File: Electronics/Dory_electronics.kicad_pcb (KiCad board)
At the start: 2 copper layers, 21 parts, among them J1 Bateria 2S, J10 SHARP_CENTRO_E, J2 Conn_01x08, J3 Conn_01x08, J4 Motor B, J5 Motor A, J6 sensor IR, J7 VL53L0X_ESQUERDO, J8 SHARP_CENTRO_D, J9 VL53L0X_DIREITO, SW1 SW_Push, U1 LM1117 5V

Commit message: chore(Electronics): organize and finish schematic
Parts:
- removed J2, J3: Conn_01x08, Connector_PinSocket_2.54mm:PinSocket_1x08_P2.54mm_Vertical
- removed SW1: SW_Push, Button_Switch_THT:Nidec_Copal_SH-7010C
- added 6_Pins_Button1: ~, Button_Switch_THT:Nidec_Copal_SH-7010C, F.Cu at (153.9, 101.0)
- added H_Bridge1: ~, esp32_devkit_v1_doit:H_Bridge, F.Cu at (170.9, 91.8)
- added R5: 4k7, Resistor_THT:R_Axial_DIN0207_L6.3mm_D2.5mm_P10.16mm_Horizontal, F.Cu at (206.0, 96.9)
- added R8: 7k5, Resistor_SMD:R_0805_2012Metric, F.Cu at (186.5, 79.9)
- R7: value 4k7 -> 15k; footprint Resistor_THT:R_Axial_DIN0207_L6.3mm_D2.5mm_P10.16mm_Horizontal -> Resistor_SMD:R_0805_2012Metric
- moved DEVKIT1 98.2 mm to (227.1, 96.7), turned to -90 degrees
- moved J9 89.4 mm to (237.5, 77.0), turned to -90 degrees
- moved J6 73.2 mm to (227.0, 72.0), turned to 90 degrees
- moved R2 64.4 mm to (220.6, 78.5), turned to 180 degrees
- moved R1 64.2 mm to (220.6, 76.0)
- moved J8 58.2 mm to (215.5, 72.0), turned to -90 degrees
- moved R6 53.0 mm to (201.5, 107.1), turned to 90 degrees
- moved R4 52.4 mm to (202.6, 78.5), turned to 180 degrees
- moved R3 52.1 mm to (202.6, 76.0)
- moved R7 44.4 mm to (183.0, 79.9), turned to -90 degrees
- moved J10 43.0 mm to (200.0, 72.0), turned to -90 degrees
- moved J1 35.5 mm to (156.5, 107.0), turned to -90 degrees
- moved U1 21.5 mm to (176.1, 70.5), turned to 180 degrees
- moved J4 17.9 mm to (166.5, 107.5)
- moved J5 15.3 mm to (177.9, 108.5), turned to 180 degrees
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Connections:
- DEVKIT1 pad 16: unconnected-(DEVKIT1-MOSI/23-Pad16) -> 3V3
- DEVKIT1 pad 17: SCL -> GND
- DEVKIT1 pad 2: ADC_CENTRO_E -> IR
- DEVKIT1 pad 20: SDA -> unconnected-(DEVKIT1-ADC2_0/4-Pad20)
- DEVKIT1 pad 21: XSHUT_E -> unconnected-(DEVKIT1-RXD_2/16-Pad21)
- DEVKIT1 pad 22: XSHUT_D -> unconnected-(DEVKIT1-TXD_2/17-Pad22)
- DEVKIT1 pad 24: unconnected-(DEVKIT1-TXD_2/17-Pad24) -> XSHUT_D
- DEVKIT1 pad 25: unconnected-(DEVKIT1-RXD_2/16-Pad25) -> XSHUT_E
- DEVKIT1 pad 26: unconnected-(DEVKIT1-ADC2_0/4-Pad26) -> SDA
- DEVKIT1 pad 29: GND -> SCL
- DEVKIT1 pad 30: 3V3 -> unconnected-(DEVKIT1-MOSI/23-Pad30)
- DEVKIT1 pad 4: IR -> ADC_CENTRO_E
- DEVKIT1 pad 5: unconnected-(DEVKIT1-ADC1_7/35-Pad5) -> (2S)/3
- DEVKIT1 pad 6: AIN1 -> BIN2
- DEVKIT1 pad 7: AIN2 -> BIN1
- DEVKIT1 pad 8: BIN1 -> AIN1
- DEVKIT1 pad 9: BIN2 -> AIN2
- R6 pad 1: SCL -> 3V3
- R6 pad 2: 3V3 -> SDA
- R7 pad 1: 3V3 -> 2S
- R7 pad 2: SDA -> (2S)/3
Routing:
- net 3V3: track 0.00 -> 218.3 mm
- net SCL: track 0.00 -> 117.9 mm
- net SDA: track 0.00 -> 112.7 mm
- net XSHUT_E: track 0.00 -> 75.0 mm
- net 5V: track 0.00 -> 63.2 mm
- net 2S: track 0.00 -> 55.8 mm
- net XSHUT_D: track 0.00 -> 47.4 mm
- net BIN2: track 0.00 -> 40.8 mm
- net BIN1: track 0.00 -> 37.2 mm
- net (2S)/3: track 0.00 -> 35.2 mm
- net AIN1: track 0.00 -> 32.6 mm
- net AIN2: track 0.00 -> 29.0 mm
- net AO1: track 0.00 -> 23.9 mm
- net ADC_CENTRO_E: track 0.00 -> 20.7 mm
- net AO2: track 0.00 -> 20.3 mm
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- added copper zone on B.Cu, net GND
- added copper zone on F.Cu, net GND
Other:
- board outline added: 90 x 45 mm

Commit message: chore: update schematic and PCB
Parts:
- moved R8 12.6 mm to (198.5, 76.1)
- moved R7 10.2 mm to (192.5, 76.1)
- moved J10 9.57 mm to (209.5, 71.0)
- moved R4 8.06 mm to (210.3, 76.1), turned to 90 degrees
- moved R6 7.89 mm to (194.0, 104.5), turned to 0 degrees
- moved J8 6.33 mm to (221.8, 71.0)
- moved U1 5.23 mm to (170.9, 71.0), turned to -90 degrees
- moved J6 5.17 mm to (229.5, 76.5), turned to 180 degrees
- moved R1 4.69 mm to (215.9, 76.1), turned to -90 degrees
- moved J7 3.50 mm to (156.4, 73.5)
- moved R2 3.15 mm to (222.6, 76.1), turned to 90 degrees
- moved R5 2.21 mm to (204.2, 98.1), turned to 180 degrees
- moved C1 2.06 mm to (164.5, 74.7)
- moved 6_Pins_Button1 1.77 mm to (154.0, 99.2)
- moved J9 1.43 mm to (238.5, 78.0)
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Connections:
- DEVKIT1 pad 24: XSHUT_D -> XSHUT_E
- DEVKIT1 pad 25: XSHUT_E -> XSHUT_D
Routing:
- net 3V3: track 218.3 -> 193.8 mm
- net XSHUT_D: track 47.4 -> 33.5 mm
- net (2S)/3: track 35.2 -> 28.5 mm
- net SCL: track 117.9 -> 124.5 mm
- net SDA: track 112.7 -> 118.8 mm
- net ADC_CENTRO_D: track 8.91 -> 14.0 mm
- net 5V: track 63.2 -> 68.3 mm
- net XSHUT_E: track 75.0 -> 71.5 mm
- net IR: track 13.0 -> 9.59 mm
- net VO_CENTRO_E: track 4.68 -> 8.07 mm
- net VO_CENTRO_D: track 5.79 -> 8.33 mm
- net AO1: track 23.9 -> 25.4 mm
- net BO1: track 10.5 -> 11.9 mm
- net AIN2: track 29.0 -> 30.3 mm
- net Net-(6_Pins_Button1-I2): track 13.6 -> 14.8 mm
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
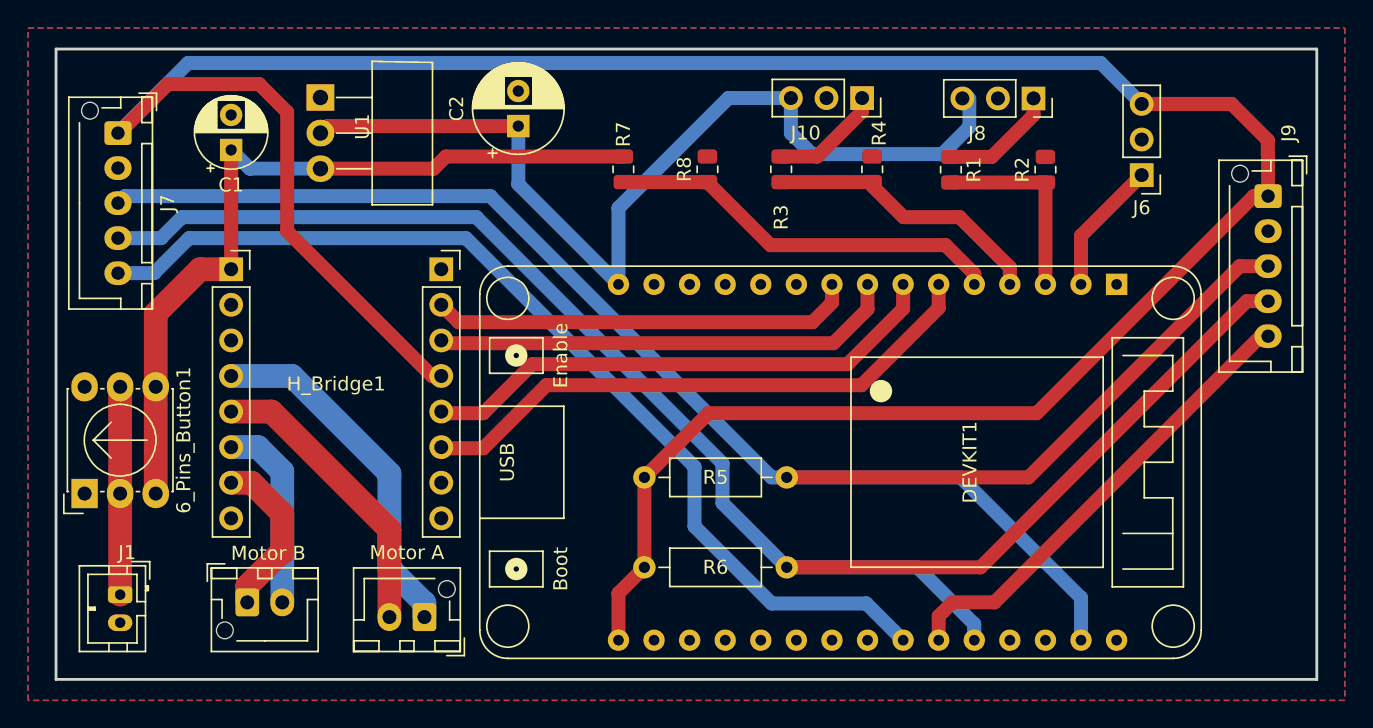
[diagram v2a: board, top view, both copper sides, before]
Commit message: chore: redo paths to homemade pcb
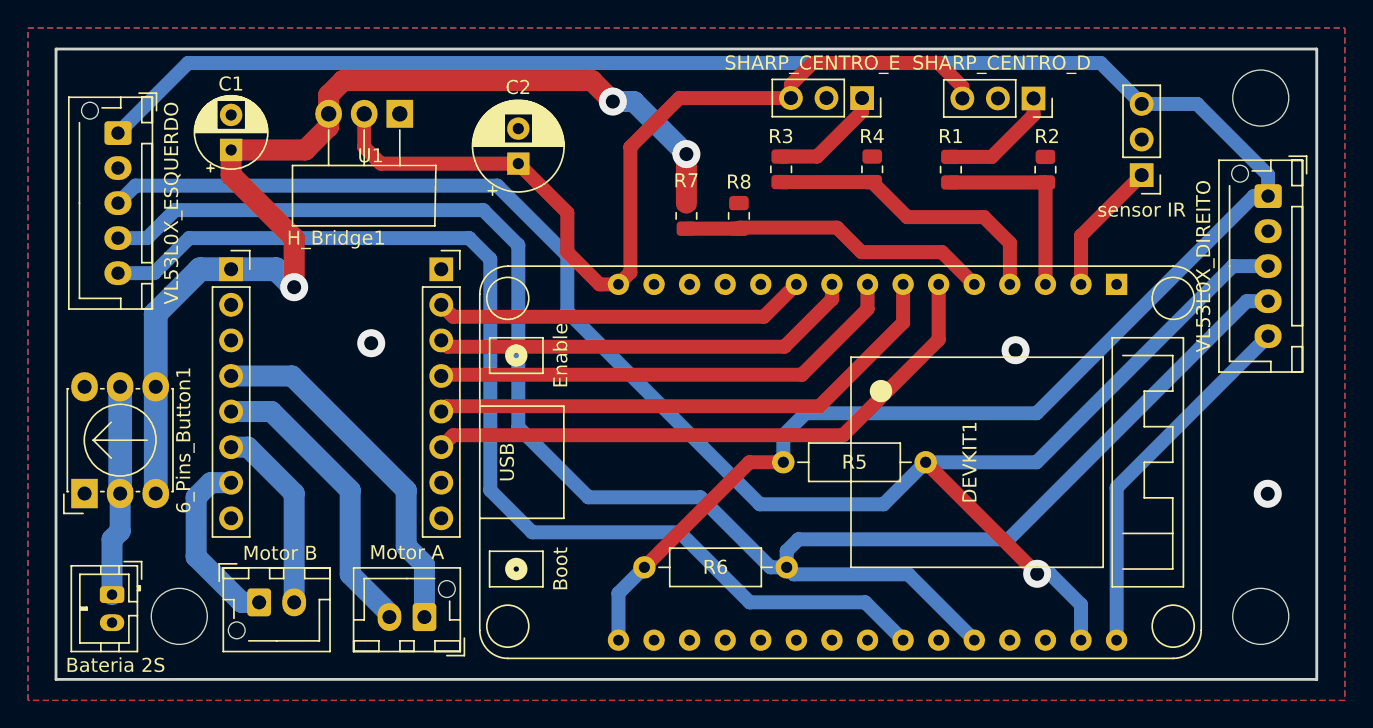
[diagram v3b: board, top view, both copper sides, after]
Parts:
- moved R5 9.98 mm to (214.1, 97.0)
- moved U1 5.78 mm to (176.5, 72.1), turned to 180 degrees
- moved R7 5.60 mm to (197.0, 79.4)
- moved R8 4.01 mm to (200.8, 79.4)
- moved C2 2.68 mm to (185.0, 75.7)
- moved J4 0.85 mm to (166.5, 107.0)
- moved J1 0.58 mm to (156.0, 106.5)
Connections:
- DEVKIT1 pad 10: unconnected-(DEVKIT1-ADC2_7/27-Pad10) -> AIN2
- DEVKIT1 pad 25: XSHUT_D -> unconnected-(DEVKIT1-MISO/19-Pad25)
- DEVKIT1 pad 30: unconnected-(DEVKIT1-MOSI/23-Pad30) -> XSHUT_D
- DEVKIT1 pad 8: AIN1 -> STDBY
- DEVKIT1 pad 9: AIN2 -> AIN1
- H_Bridge1 pad 13: 3V3 -> STDBY
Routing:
- net 3V3: track 193.8 -> 151.6 mm
- net STDBY: track 0.00 -> 34.2 mm
- net 2S: track 57.0 -> 77.8 mm, vias 0 -> 3
- net XSHUT_D: track 33.5 -> 26.2 mm
- net XSHUT_E: track 71.5 -> 78.6 mm
- net SDA: track 118.8 -> 125.2 mm
- net (2S)/3: track 28.5 -> 22.3 mm
- net SCL: track 124.5 -> 119.3 mm, vias 0 -> 1
- net 5V: track 68.3 -> 64.7 mm
- net AIN2: track 30.3 -> 26.7 mm
- net AIN1: track 33.3 -> 30.8 mm
- net BIN2: track 41.4 -> 42.6 mm
- net BO1: track 11.9 -> 13.0 mm
- net ADC_CENTRO_E: track 20.2 -> 21.1 mm
- net GND: vias 0 -> 3
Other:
- outline, holes or cut-outs redrawn
- board text added: "Solda só a parte de cima"

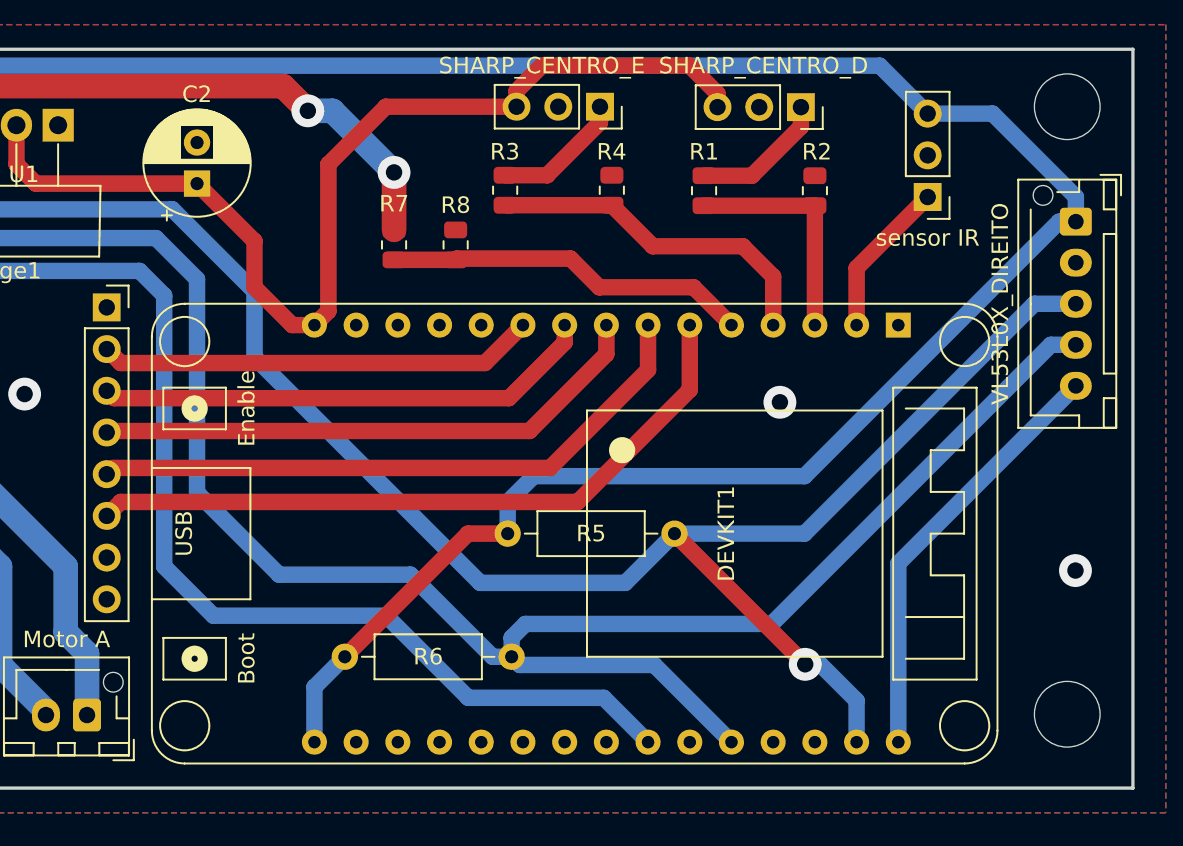
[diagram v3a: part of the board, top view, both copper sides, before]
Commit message: chore: update esp32 lib sym and footprint
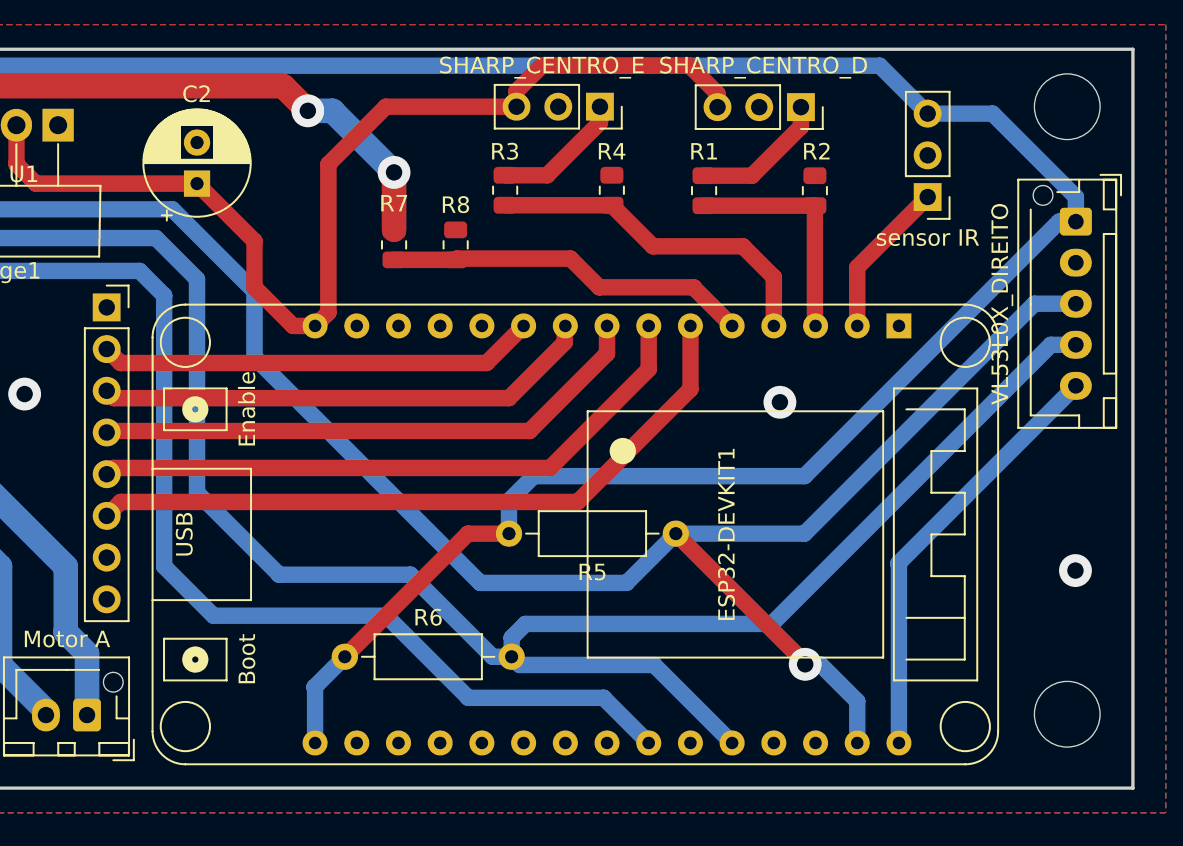
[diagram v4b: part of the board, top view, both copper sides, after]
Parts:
- removed DEVKIT1: ESP, esp32_devkit_v1_doit:esp32_devkit_v1_doit
- added ESP32-DEVKIT1: ~, esp32_devkit_v1_doit:esp32_devkit_v1_doit, F.Cu at (227.8, 97.0)
- moved R5 0.08 mm to (214.2, 97.0)

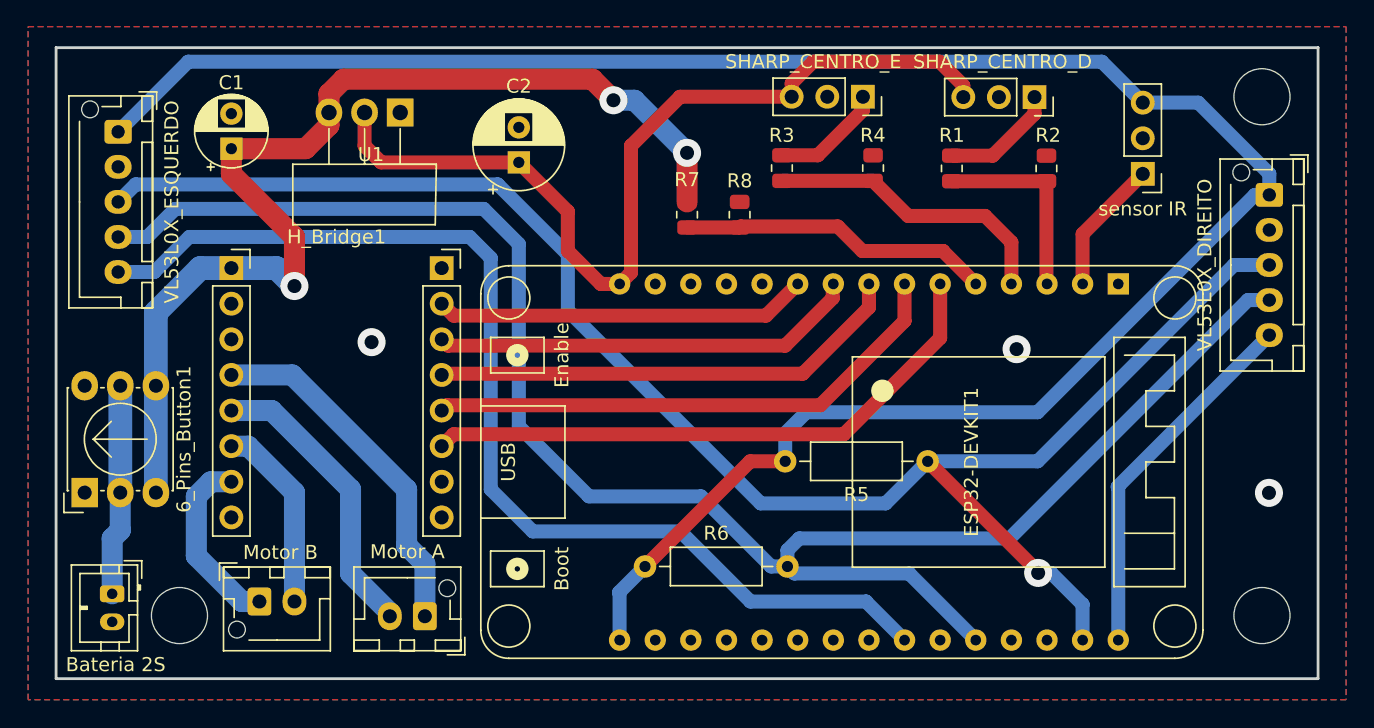
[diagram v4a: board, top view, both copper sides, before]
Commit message: chore: Add/Update 3D models on PCB
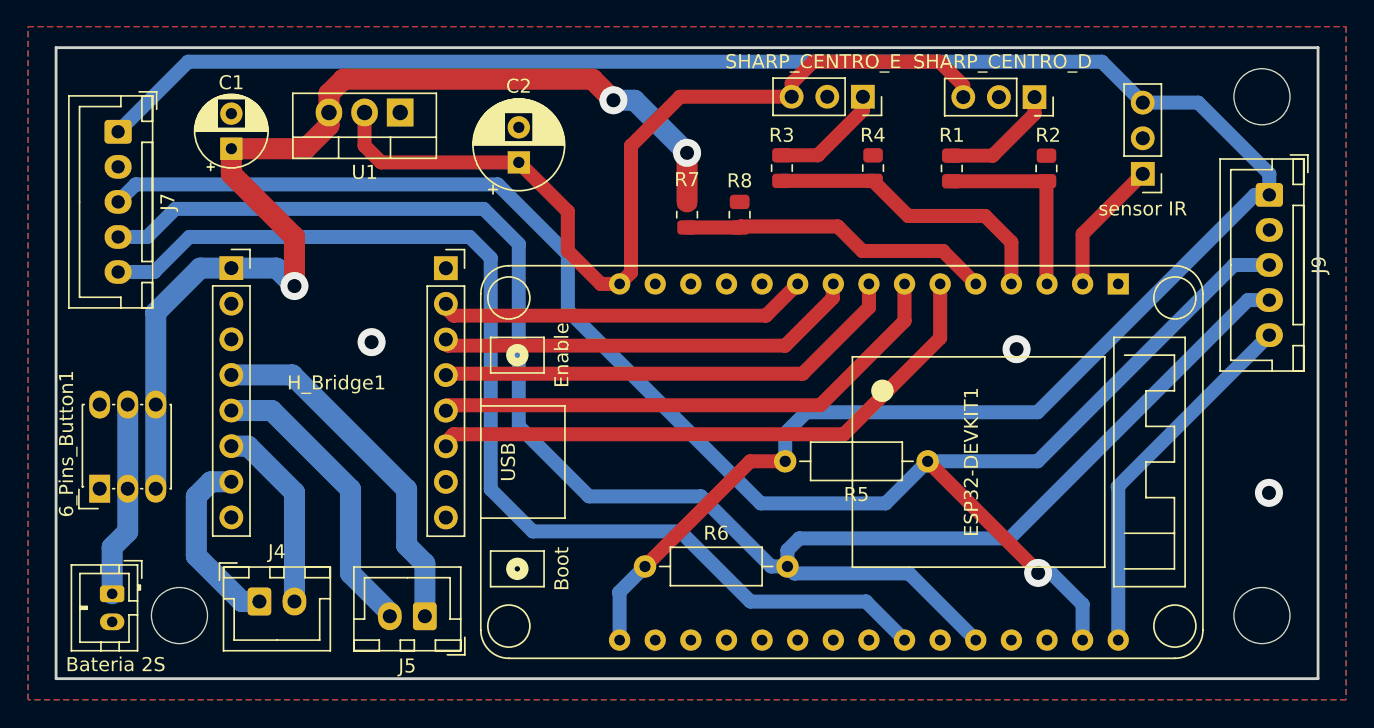
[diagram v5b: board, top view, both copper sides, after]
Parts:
- 6_Pins_Button1: footprint Button_Switch_THT:Nidec_Copal_SH-7010C -> esp32_devkit_v1_doit:Push_Button_6_pins
- ESP32-DEVKIT1: footprint esp32_devkit_v1_doit:esp32_devkit_v1_doit -> esp32_devkit_v1_doit:esp32_with_headers
- H_Bridge1: footprint esp32_devkit_v1_doit:H_Bridge -> esp32_devkit_v1_doit:H_Bridge_with_headers
- J4, J5: footprint Connector_JST:JST_XH_B2B-XH-AM_1x02_P2.50mm_Vertical -> Connector_JST:JST_XH_B2B-XH-A_1x02_P2.50mm_Vertical
- J7, J9: footprint Connector_JST:JST_XH_B5B-XH-AM_1x05_P2.50mm_Vertical -> Connector_JST:JST_XH_B5B-XH-A_1x05_P2.50mm_Vertical
- U1: footprint Package_TO_SOT_THT:TO-220-3_Horizontal_TabDown -> Package_TO_SOT_THT:TO-220-3_Vertical
- moved 6_Pins_Button1 1.11 mm to (155.1, 99.0)
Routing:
- net Net-(6_Pins_Button1-I2): track 15.1 -> 14.0 mm

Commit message: chore: update PCB and create BOM file
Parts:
- R1, R2, R3, R4, R7, R8: moved to B.Cu
- moved J9 94.5 mm to (158.6, 128.4), turned to 180 degrees
- moved ESP32-DEVKIT1 87.2 mm to (142.9, 117.2), turned to 180 degrees
- moved J6 80.7 mm to (161.1, 119.4), turned to 90 degrees
- moved R5 80.2 mm to (135.9, 114.5), turned to 90 degrees
- moved R2 72.2 mm to (159.9, 111.9)
- moved J8 68.9 mm to (165.6, 110.9), turned to 180 degrees
- moved J5 65.1 mm to (126.9, 68.1), turned to 90 degrees
- moved R1 64.4 mm to (162.4, 111.9)
- moved J4 63.7 mm to (127.9, 56.4), turned to -90 degrees
- moved J1 62.8 mm to (135.4, 47.1), turned to 180 degrees
- moved R4 55.9 mm to (159.9, 100.4)
- moved 6_Pins_Button1 55.5 mm to (140.7, 45.4), turned to 0 degrees
- moved J10 52.3 mm to (165.6, 99.4), turned to 180 degrees
- moved R6 49.4 mm to (144.6, 104.3), turned to -90 degrees
- moved R3 48.0 mm to (162.4, 100.4)
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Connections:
- J7 pad 3: SCL -> SDA
- J7 pad 4: SDA -> SCL
- J9 pad 3: SCL -> SDA
- J9 pad 4: SDA -> SCL
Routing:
- net 2S: track 77.5 -> 61.5 mm, vias 3 -> 0
- net SDA: track 125.3 -> 109.3 mm, vias 0 -> 1
- net SCL: track 119.3 -> 105.1 mm
- net XSHUT_E: track 78.7 -> 66.9 mm, vias 0 -> 2
- net 5V: track 64.8 -> 56.4 mm, vias 0 -> 2
- net ADC_CENTRO_E: track 21.1 -> 13.6 mm
- net ADC_CENTRO_D: track 14.1 -> 7.03 mm
- net VO_CENTRO_D: track 8.33 -> 3.27 mm
- net VO_CENTRO_E: track 8.07 -> 3.27 mm
- net BIN2: track 42.6 -> 46.2 mm
- net BIN1: track 38.3 -> 41.8 mm
- net STDBY: track 34.1 -> 37.3 mm
- net (2S)/3: track 22.3 -> 25.4 mm
- net Net-(6_Pins_Button1-I2): track 14.0 -> 11.4 mm
- net AIN1: track 30.8 -> 33.1 mm
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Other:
- board size 90 x 45 mm -> 45 x 90 mm
- board text removed: "Solda só a parte de cima"
